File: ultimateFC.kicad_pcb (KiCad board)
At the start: 8 copper layers, 30.4 x 25.2 mm, 190 parts, among them J1 USB_B_Micro, J2 10132797-011100LF, J3 10132797-011100LF, J4 10132797-011100LF, J5 10132797-011100LF, J6 10132797-011100LF, Q1 DMP2066LSN-7, U1 EFM8BB21F16G-C-QFN20R, U10 NCP81253MNTBG, U11 SiZ200DT, U12 NCP81253MNTBG, U13 SiZ200DT, U14 TPS62824ADMQ, U15 SiZ200DT, U16 NCP81253MNTBG, U17 NCP81253MNTBG, U18 NCP81253MNTBG, U19 NCP81253MNTBG, U2 EFM8BB21F16G-C-QFN20R, U20 SiZ200DT, U21 SiZ200DT, U22 SiZ200DT, U23 SiZ200DT, U24 EFM8BB21F16G-C-QFN20R, U25 NCP81253MNTBG, U26 SiZ200DT, U27 NCP81253MNTBG, U28 NCP81253MNTBG, U29 SiZ200DT, U3 NCP81253MNTBG, U30 SiZ200DT, U31 INA186, U33 STM32F745VGHx, U34 AB7456, U35 ZOE-M8Q_ZOE-M8Q, U36 ICM-20602, U37 S25FL064L, U39 BMP280, U4 SiZ200DT, U5 TPS630701, U6 EFM8BB21F16G-C-QFN20R, U7 NCP81253MNTBG, U8 SiZ200DT, U9 NCP81253MNTBG, X1 Molex_734120110, Y1 CSTNE8M00G550000R0, Y2 ECS-270-8-47Q-CES-TR

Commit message: update layout
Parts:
- removed the REF** at (197.1, 64.2) (x2)
- added REF**: Fiducial_0.5mm_Dia_1mm_Outer, Fiducial:Fiducial_0.5mm_Dia_1mm_Outer, F.Cu at (197.1, 64.2)
- added REF**: Fiducial_0.5mm_Dia_1mm_Outer, Fiducial:Fiducial_0.5mm_Dia_1mm_Outer, B.Cu at (197.1, 64.2)

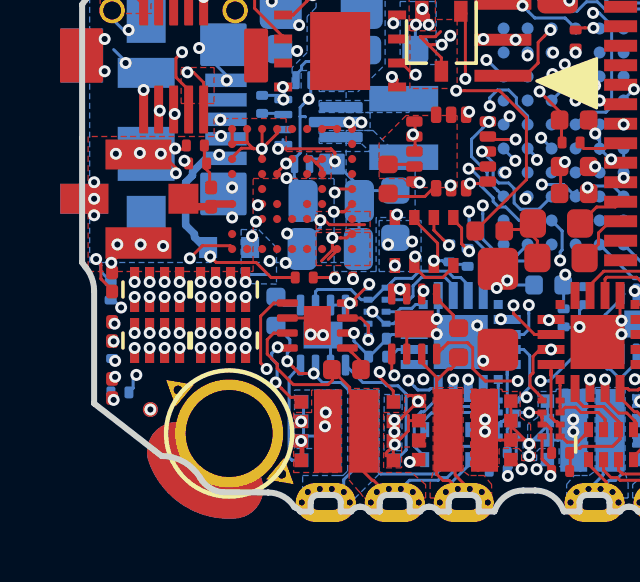
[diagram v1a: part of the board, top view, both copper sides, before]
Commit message: update footprints to reflect surface mounting update lib update assembly_output/*.pos
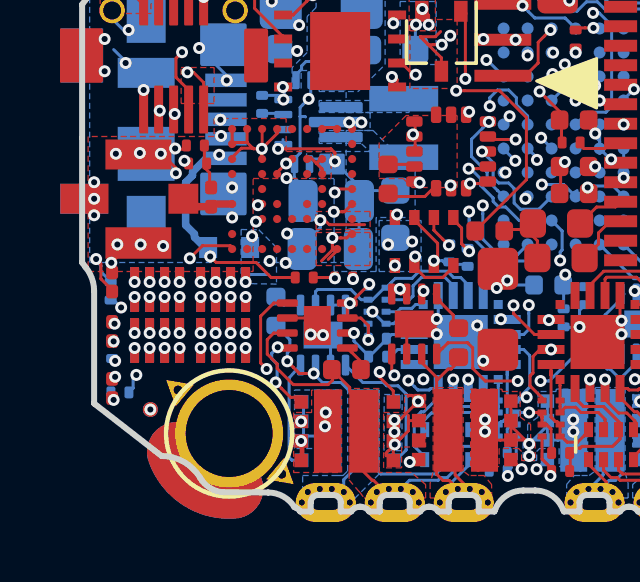
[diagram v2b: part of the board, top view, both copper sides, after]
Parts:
- removed the REF** at (197.1, 64.2) (x2)
- added REF**: Fiducial_0.5mm_Dia_1mm_Outer, Fiducial:Fiducial_0.5mm_Dia_1mm_Outer, F.Cu at (197.1, 64.2)
- added REF**: Fiducial_0.5mm_Dia_1mm_Outer, Fiducial:Fiducial_0.5mm_Dia_1mm_Outer, B.Cu at (197.1, 64.2)
- moved C14 0.10 mm to (172.3, 78.9)
- moved C41 0.10 mm to (172.3, 77.2)
- moved C15 0.10 mm to (170.1, 78.9)
- moved C20 0.10 mm to (172.3, 78.9)
- moved C21 0.10 mm to (170.1, 77.2)
- moved C42 0.10 mm to (170.1, 77.2)
- moved C43 0.10 mm to (172.3, 77.2)
- moved C44 0.10 mm to (170.1, 78.9)

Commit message: fix fidu centers, update pos files
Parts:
- removed the REF** at (197.1, 64.2) (x2)
- removed the REF** at (169.8, 81.2)
- added REF**: Fiducial_0.5mm_Dia_1mm_Outer, Fiducial:Fiducial_0.5mm_Dia_1mm_Outer, F.Cu at (197.2, 64.2)
- added REF**: Fiducial_0.5mm_Dia_1mm_Outer, Fiducial:Fiducial_0.5mm_Dia_1mm_Outer, B.Cu at (197.2, 64.2)
- added REF**: Fiducial_0.5mm_Dia_1mm_Outer, Fiducial:Fiducial_0.5mm_Dia_1mm_Outer, B.Cu at (169.9, 81.2)
- moved REF** 0.07 mm to (169.9, 81.2)
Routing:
- net GND: track 143.1 -> 151.1 mm
- net +5V: track 35.8 -> 39.8 mm
- net +3V3: track 27.8 -> 31.6 mm
